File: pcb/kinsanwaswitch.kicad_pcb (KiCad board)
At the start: 2 copper layers, 26 x 15.5 mm, 8 parts, among them J1 Conn_01x05, J2 Conn_01x02, U1 74LVC1G14

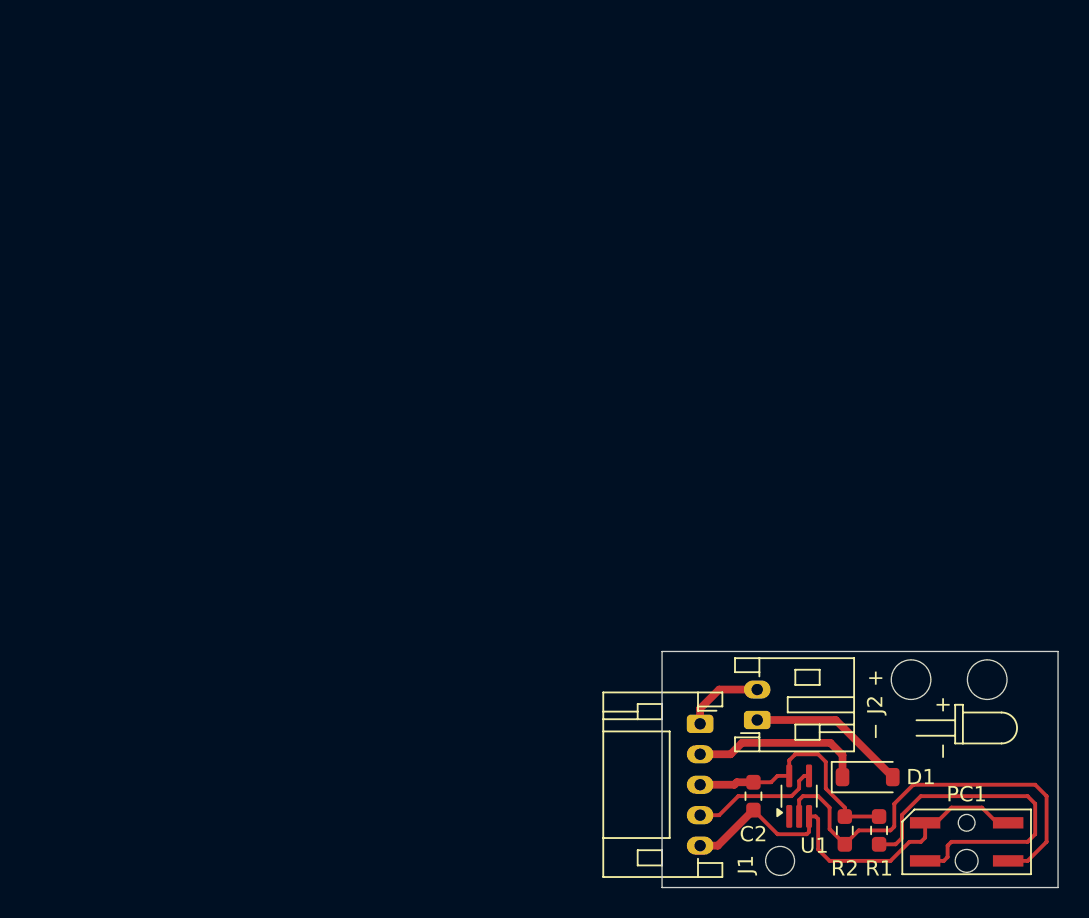
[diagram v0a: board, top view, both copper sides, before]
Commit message: add name and dates to sheets
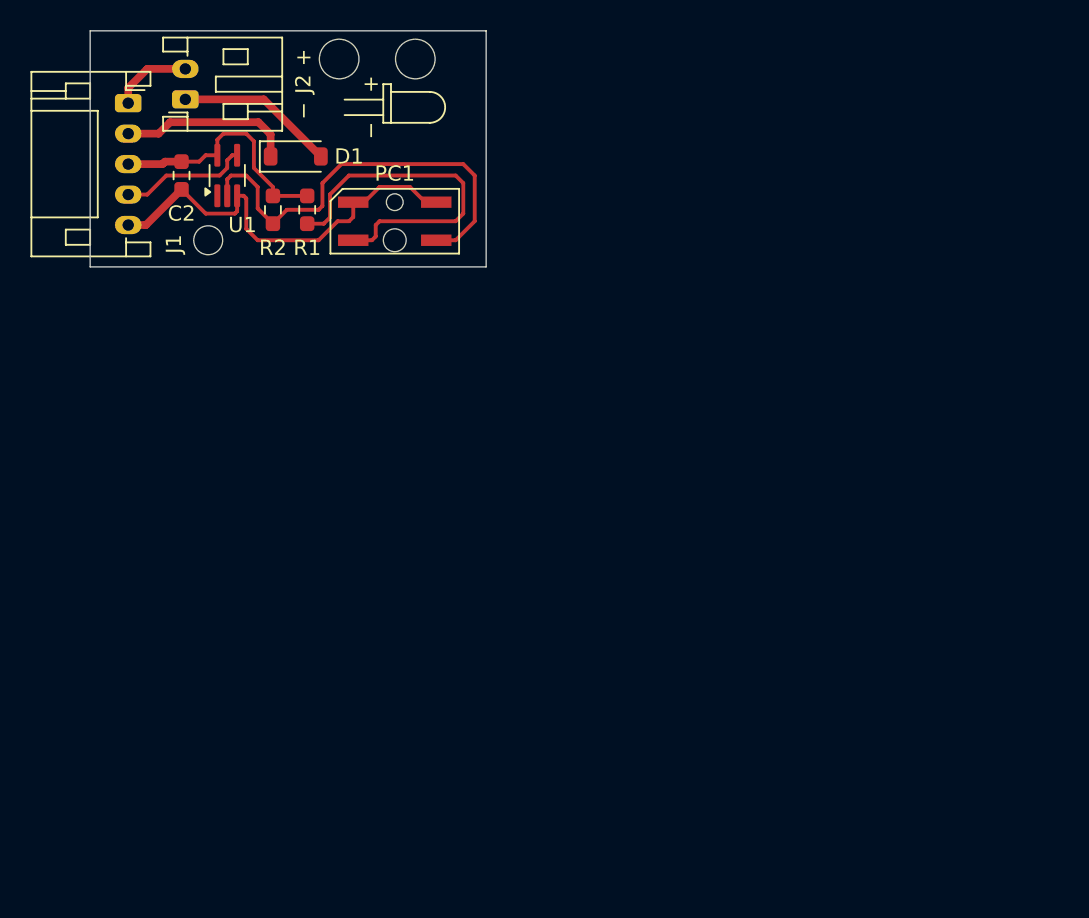
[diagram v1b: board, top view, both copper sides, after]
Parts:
- moved C2 55.4 mm to (95.2, 67.0)
- moved D1 55.4 mm to (102.7, 65.8)
- moved J1 55.4 mm to (91.7, 62.2)
- moved J2 55.4 mm to (95.5, 62.0)
- moved PC1 55.4 mm to (109.2, 70.0)
- moved R1 55.4 mm to (103.5, 69.2)
- moved R2 55.4 mm to (101.2, 69.2)
- moved U1 55.4 mm to (98.2, 67.0)
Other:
- outline, holes or cut-outs redrawn

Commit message: revision 1.0 PCB
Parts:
- removed D1: NSI45020AT1G, Diode_SMD:D_SOD-123
- removed J2: Conn_01x02, Connector_JST:JST_PH_S2B-PH-K_1x02_P2.00mm_Horizontal
- added C1: 1u0, Capacitor_SMD:C_0603_1608Metric, F.Cu at (102.7, 78.0)
- added C3: 100n, Capacitor_SMD:C_0603_1608Metric, F.Cu at (106.7, 80.0)
- added D2: 1N5819HW-7-F, Diode_SMD:D_SOD-123, F.Cu at (101.9, 74.6)
- added FID1: Fiducial, Fiducial:Fiducial_0.5mm_Mask1mm, F.Cu at (89.9, 69.8)
- added FID2: Fiducial, Fiducial:Fiducial_0.5mm_Mask1mm, F.Cu at (118.4, 86.2)
- added R3: 10R, Resistor_SMD:R_0603_1608Metric, F.Cu at (108.3, 78.2)
- added SYM1: Logo_Open_Hardware_Small, Symbol:OSHW-Logo_5.7x6mm_SilkScreen, B.Cu at (92.2, 83.8)
- C2: footprint Resistor_SMD:R_0603_1608Metric_Pad0.98x0.95mm_HandSolder -> Capacitor_SMD:C_0603_1608Metric
- J1: value Conn_01x05 -> SM05B-PASS-TBT; footprint Connector_JST:JST_PH_S5B-PH-K_1x05_P2.00mm_Horizontal -> Connector_JST_PA:JST_PH_S5B-PH-SM4-TB_1x05-1MP_P2.00mm_Horizontal
- PC1: value RPI-352 -> RPI-0352E
- R1: footprint Resistor_SMD:R_0603_1608Metric_Pad0.98x0.95mm_HandSolder -> Resistor_SMD:R_0603_1608Metric
- R2: value 2K2 -> 47k; footprint Resistor_SMD:R_0603_1608Metric_Pad0.98x0.95mm_HandSolder -> Resistor_SMD:R_0603_1608Metric
- U1: value 74LVC1G14 -> 74HCT1G14; footprint Package_TO_SOT_SMD:SOT-353_SC-70-5_Handsoldering -> Package_TO_SOT_SMD:SC-74A-5_1.55x2.9mm_P0.95mm
- moved R1 16.9 mm to (117.4, 78.8)
- moved J1 15.9 mm to (94.1, 78.0)
- moved R2 14.3 mm to (111.9, 78.8)
- moved PC1 14.0 mm to (114.7, 82.8), turned to 180 degrees
- moved U1 12.5 mm to (107.4, 75.5), turned to 0 degrees
- moved C2 12.4 mm to (104.2, 75.5)
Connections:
- J1 pad 3: VCC -> +5V
- J1 pad 4: /OUTPUT -> /N.O.
- U1 pad 4: /OUTPUT -> Net-(R3-Pad1)
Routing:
- net /N.O.: track 0.00 -> 39.2 mm
- net GND: track 27.7 -> 0.00 mm, vias 0 -> 45
- net Net-(PC1-Pad2): track 23.0 -> 2.00 mm
- net Net-(PC1-Pad3): track 28.4 -> 11.2 mm
- net /LED-: track 11.4 -> 0.00 mm
- net Net-(J2-Pin_1): track 10.5 -> 0.00 mm
- net /OUTPUT: track 8.51 -> 0.00 mm
- net +5V: track 0.00 -> 5.90 mm
- net /LED+: track 5.27 -> 0.00 mm
- net VCC: track 16.2 -> 21.0 mm
- net Net-(R3-Pad1): track 0.00 -> 2.01 mm
- added copper zone on B.Cu, net GND
- added copper zone on F.Cu, net GND
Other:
- board size 26 x 15.5 mm -> 32 x 20 mm
- board text added: "${COMPANY}"
- board text added: "0.2540 mm / 0.2540 mm"
- board text added: "0.4000 mm"
- board text added: "0.8000 mm"
- board text added: "2"
- board text added: "32.0000 mm x 20.0000 mm"
- board text added: "BOARD CHARACTERISTICS"
- board text added: "Board Thickness:"
- board text added: "Board overall dimensions:"
- board text added: "Castellated pads:"
- board text added: "Copper Finish:"
- board text added: "Copper Layer Count:"
- board text added: "Edge card connectors:"
- board text added: "HAL lead-free"
- board text added: "Impedance Control:"
- board text added: "KinSanwaSwitch Rev. ${REVISION} ${ISSUE_DATE}"
- board text added: "Min hole diameter:"
- board text added: "Min track/spacing:"
- board text added: "No"
- board text added: "Plated Board Edge:"
- board text removed: "+"
- board text removed: "-"
- board text removed: "GND"
- board text removed: "KINSANWASWITCH Alexander Knapik Based off SHINSANWASWITCH steelpuxnastik/Doctopus"
- board text removed: "LED+"
- board text removed: "LED-"
- board text removed: "OUT"
- board text removed: "VCC"
- board text removed: "−"
